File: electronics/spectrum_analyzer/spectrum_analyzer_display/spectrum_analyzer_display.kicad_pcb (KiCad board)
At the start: 2 copper layers, 99.1 x 66 mm, 20 parts, among them J1 Conn_01x10_Pin, J2 Conn_01x14_Pin

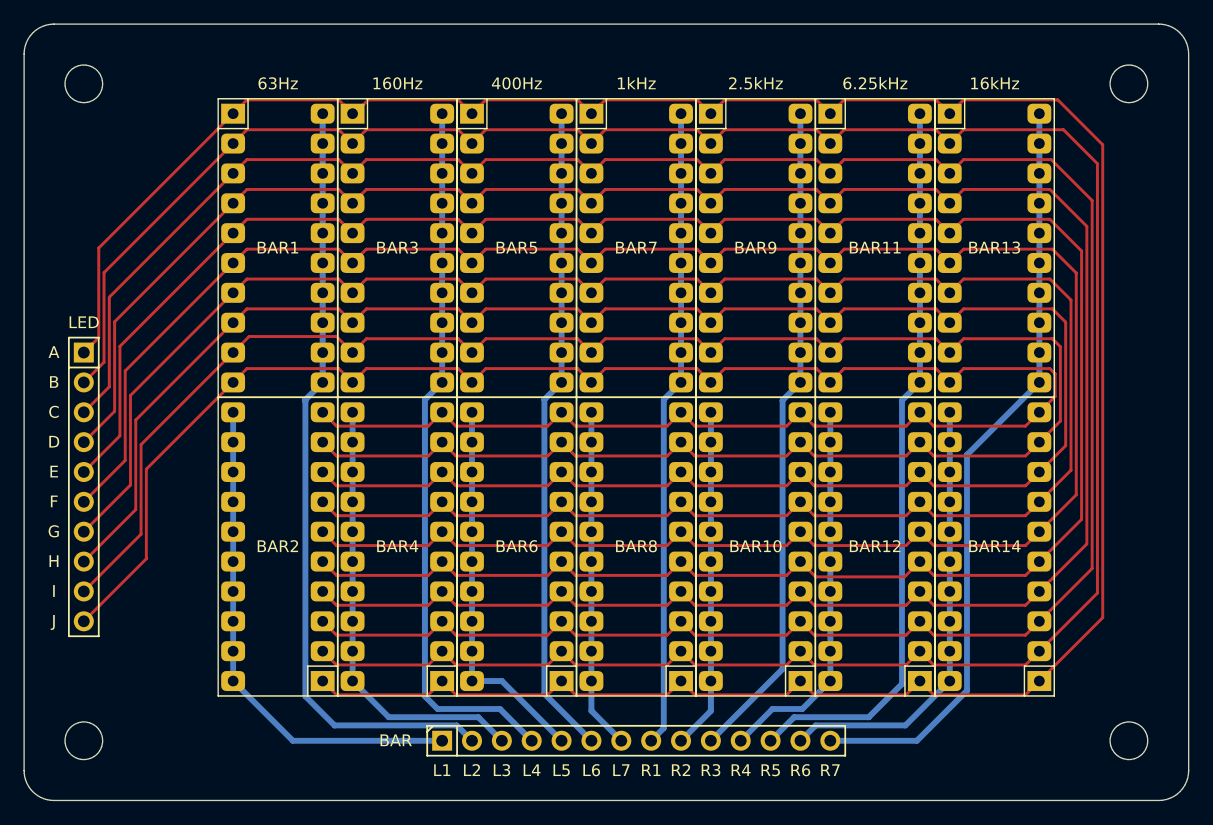
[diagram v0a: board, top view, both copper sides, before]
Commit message: feat: change wire width
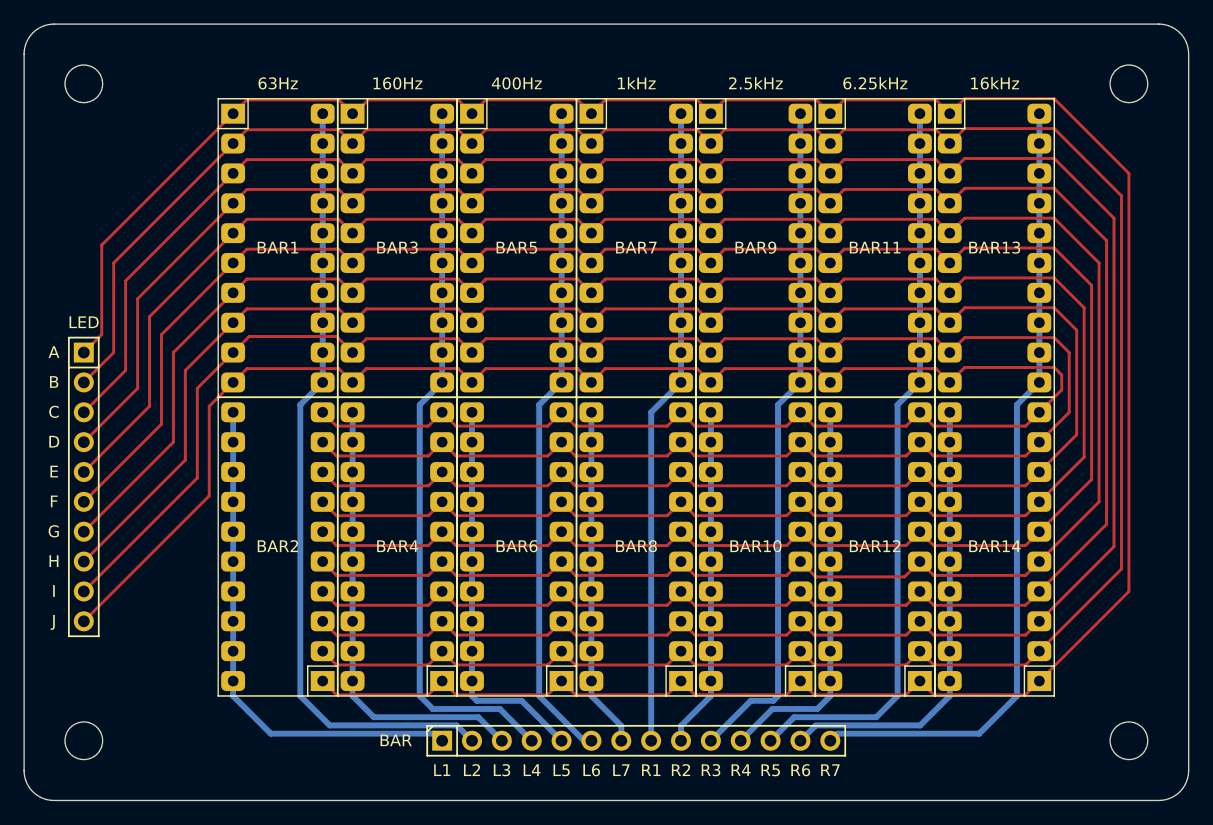
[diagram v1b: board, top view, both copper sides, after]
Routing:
- net /LEFT_7: track 65.0 -> 67.8 mm
- net /C: track 210.9 -> 212.7 mm
- net /A: track 222.3 -> 224.1 mm
- net /D: track 205.4 -> 207.1 mm
- net /E: track 200.0 -> 201.6 mm
- net /B: track 216.9 -> 218.3 mm
- net /F: track 194.6 -> 195.9 mm
- net /G: track 189.0 -> 190.3 mm
- net /LEFT_5: track 56.5 -> 57.6 mm
- net /H: track 183.7 -> 184.7 mm
- net /I: track 178.4 -> 179.2 mm
- net /J: track 172.6 -> 173.5 mm
- net /RIGHT_7: track 37.7 -> 38.4 mm
- net /RIGHT_6: track 32.6 -> 33.3 mm
- net /RIGHT_3: track 32.6 -> 33.3 mm
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
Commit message: feat: change pcb layout and enclosure design
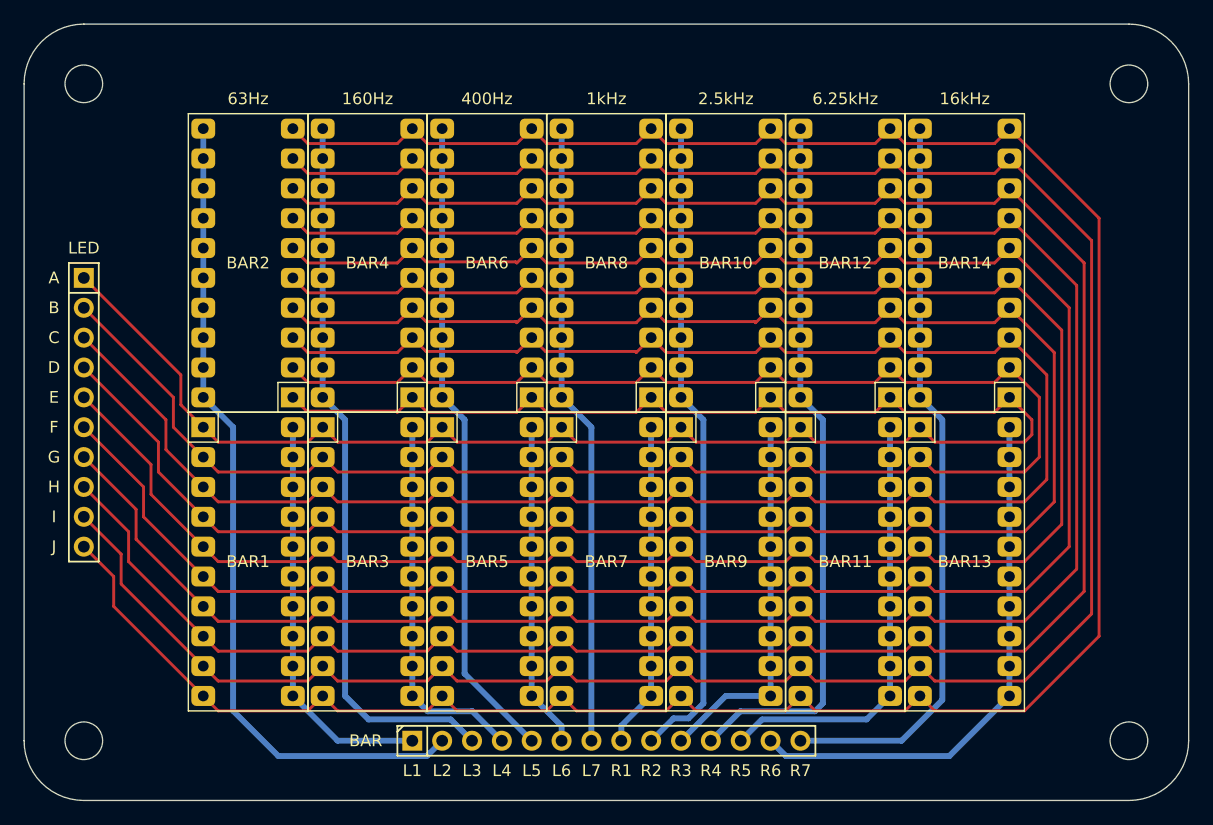
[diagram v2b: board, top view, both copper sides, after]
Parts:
- moved BAR1 26.8 mm to (68.6, 64.8)
- moved BAR11 26.8 mm to (119.4, 64.8)
- moved BAR13 26.8 mm to (129.5, 64.8)
- moved BAR3 26.8 mm to (78.7, 64.8)
- moved BAR9 26.8 mm to (109.2, 64.8)
- moved BAR5 26.8 mm to (88.9, 64.8)
- moved BAR7 26.8 mm to (99.1, 64.8)
- moved BAR4 24.3 mm to (86.4, 62.2)
- moved BAR6 24.3 mm to (96.5, 62.2)
- moved BAR10 24.3 mm to (116.8, 62.2)
- moved BAR12 24.3 mm to (127.0, 62.2)
- moved BAR14 24.3 mm to (137.2, 62.2)
- moved BAR2 24.3 mm to (76.2, 62.2)
- moved BAR8 24.3 mm to (106.7, 62.2)
- moved J1 6.35 mm to (58.4, 52.1)
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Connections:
- J2 pad 1: /RIGHT_1 -> /LEFT_1
- J2 pad 13: /RIGHT_7 -> /LEFT_7
- J2 pad 14: /LEFT_7 -> /RIGHT_7
- J2 pad 2: /LEFT_1 -> /RIGHT_1
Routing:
- net /A: track 224.1 -> 165.7 mm
- net /B: track 218.3 -> 171.3 mm
- net /J: track 173.5 -> 216.2 mm
- net /C: track 212.7 -> 176.9 mm
- net /LEFT_1: track 66.5 -> 34.6 mm
- net /I: track 179.2 -> 210.6 mm
- net /LEFT_2: track 61.4 -> 32.1 mm
- net /LEFT_3: track 56.3 -> 27.7 mm
- net /RIGHT_6: track 33.3 -> 60.5 mm
- net /RIGHT_1: track 43.5 -> 70.5 mm
- net /LEFT_4: track 54.4 -> 27.7 mm
- net /RIGHT_5: track 29.0 -> 55.4 mm
- net /LEFT_6: track 62.7 -> 37.1 mm
- net /LEFT_5: track 57.6 -> 32.1 mm
- net /D: track 207.1 -> 182.6 mm
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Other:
- outline, holes or cut-outs redrawn
